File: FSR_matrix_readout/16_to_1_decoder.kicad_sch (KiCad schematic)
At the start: 6 parts, among them U14 SN74AHC138RGYR, U15 SN74AHC138RGYR, U16 SN74LVC1G14DCKR_C19829630

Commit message: done sense opamp module
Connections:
- net GND: now also U14.17 (EP), U15.17 (EP)
- no-connect marks 3 -> 1
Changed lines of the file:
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@@
+	)
+	(junction
+		(at 116.84 43.18)
+		(diameter 0)
+		(color 0 0 0 0)
 	)
 	(junction
@@
 	)
 	(junction
+		(at 118.11 78.74)
+		(diameter 0)
+		(color 0 0 0 0)
+	)
+	(junction
 		(at 116.84 49.53)
 		(diameter 0)
@@
 	)
 	(no_connect
-		(at 111.76 82.55)
-	)
-	(no_connect
 		(at 92.71 120.65)
-	)
-	(no_connect
-		(at 111.76 46.99)
 	)
 	(bus_entry
@@
 	(wire
 		(pts
+			(xy 113.03 43.18) (xy 116.84 43.18)
+		)
+		(stroke
+			(width 0)
+			(type default)
+		)
+	)
+	(wire
+		(pts
+			(xy 113.03 46.99) (xy 113.03 43.18)
+		)
+		(stroke
+			(width 0)
+			(type default)
+		)
+	)
+	(wire
+		(pts
 			(xy 91.44 64.77) (xy 85.09 64.77)
 		)
@@
 	(wire
 		(pts
+			(xy 114.3 78.74) (xy 118.11 78.74)
+		)
+		(stroke
+			(width 0)
+			(type default)
+		)
+	)
+	(wire
+		(pts
+			(xy 111.76 46.99) (xy 113.03 46.99)
+		)
+		(stroke
+			(width 0)
+			(type default)
+		)
+	)
+	(wire
+		(pts
 			(xy 88.9 97.79) (xy 91.44 97.79)
 		)
@@
 	(wire
 		(pts
+			(xy 114.3 82.55) (xy 111.76 82.55)
+		)
+		(stroke
+			(width 0)
+			(type default)
+		)
+	)
+	(wire
+		(pts
 			(xy 88.9 58.42) (xy 91.44 58.42)
 		)
@@
 		(pts
 			(xy 85.09 100.33) (xy 85.09 106.68)
+		)
+		(stroke
+			(width 0)
+			(type default)
+		)
+	)
+	(wire
+		(pts
+			(xy 114.3 82.55) (xy 114.3 78.74)
 		)
 		(stroke
@@
 		(in_pos_files yes)
 		(dnp no)
-		(property "Reference" "#PWR?"
+		(property "Reference" "#PWR056"
 			(at 85.09 102.87 0)
 			(hide yes)
@@
 			(project "FSR_matrix_readout"
 				(path "/6dca5e5c-f676-465d-98c9-14af6047a226/41800b67-536b-40f6-9870-7d633bd400f6"
-					(reference "#PWR?")
+					(reference "#PWR056")
 					(unit 1)
 				)
@@
 		(instances
 			(project "FSR_matrix_readout"
-				(path "/6dca5e5c-f676-465d-98c9-14af6047a226"
-					(reference "U16")
-					(unit 1)
-				)
 				(path "/6dca5e5c-f676-465d-98c9-14af6047a226/41800b67-536b-40f6-9870-7d633bd400f6"
 					(reference "U16")
@@
 		(dnp no)
 		(fields_autoplaced yes)
-		(property "Reference" "#PWR?"
+		(property "Reference" "#PWR057"
 			(at 86.36 125.73 0)
 			(hide yes)
@@
 			(project "FSR_matrix_readout"
 				(path "/6dca5e5c-f676-465d-98c9-14af6047a226/41800b67-536b-40f6-9870-7d633bd400f6"
-					(reference "#PWR?")
+					(reference "#PWR057")
 					(unit 1)
 				)
@@
 		(instances
 			(project "FSR_matrix_readout"
-				(path "/6dca5e5c-f676-465d-98c9-14af6047a226"
-					(reference "U14")
-					(unit 1)
-				)
 				(path "/6dca5e5c-f676-465d-98c9-14af6047a226/41800b67-536b-40f6-9870-7d633bd400f6"
 					(reference "U14")

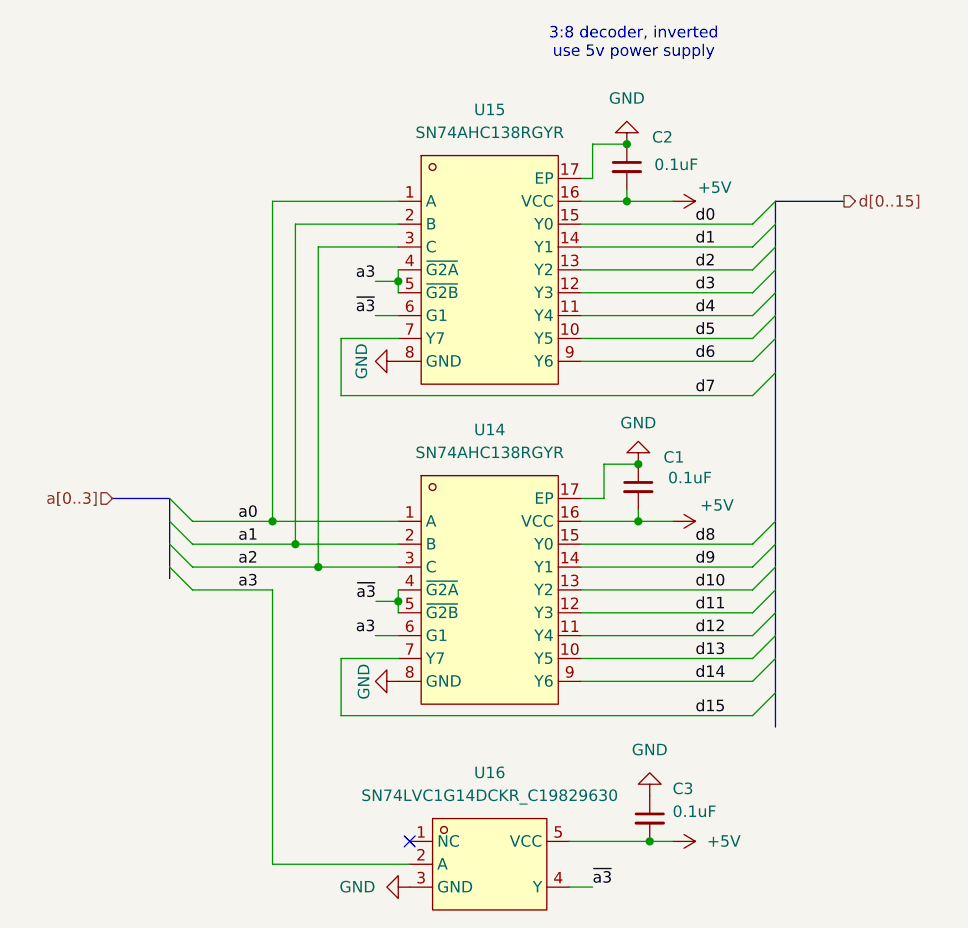
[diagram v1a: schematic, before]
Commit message: remove all ERC errors
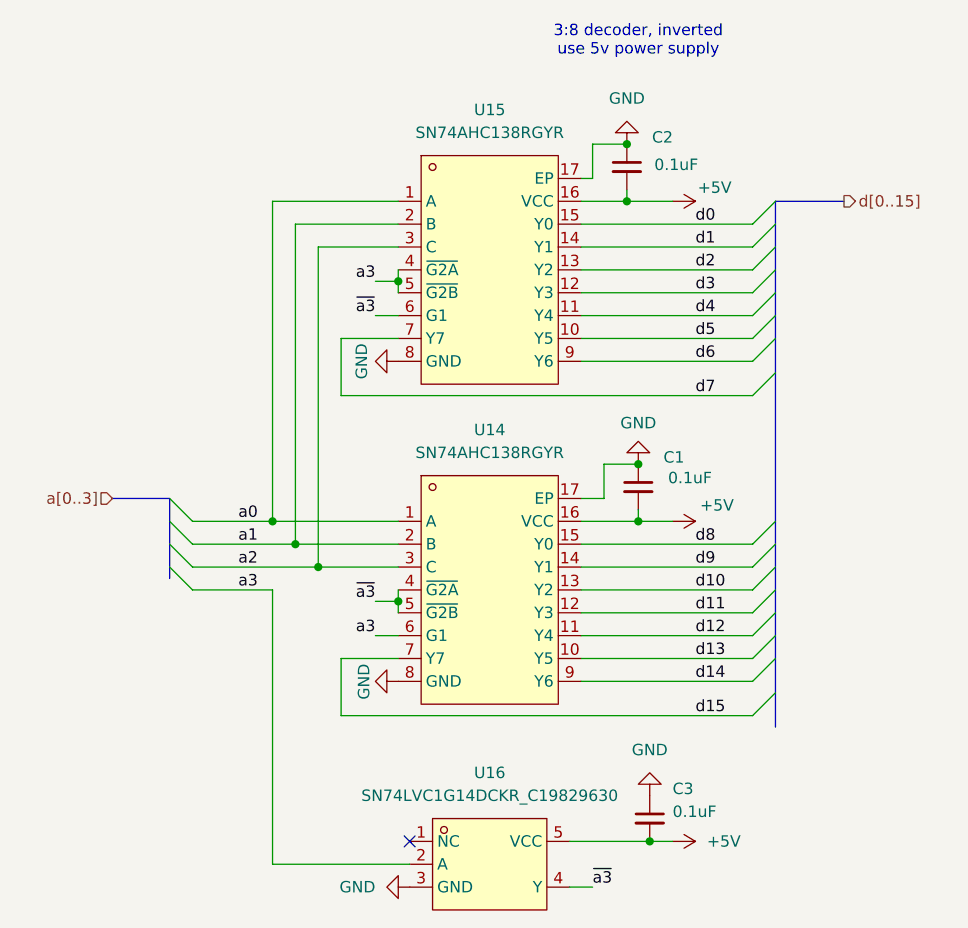
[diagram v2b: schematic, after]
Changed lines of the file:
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@@
 	(text "3:8 decoder, inverted\nuse 5v power supply"
 		(exclude_from_sim no)
-		(at 117.602 32.004 0)
+		(at 118.11 31.75 0)
 		(effects
 			(font
@@
 	(wire
 		(pts
-			(xy 88.9566 93.98) (xy 91.44 93.98)
+			(xy 88.9 93.98) (xy 91.44 93.98)
 		)
 		(stroke
@@
 	)
 	(label "~{a3}"
-		(at 88.9566 93.98 180)
-		(effects
-			(font
+		(at 88.9 93.98 180)
+		(effects
+			(font
